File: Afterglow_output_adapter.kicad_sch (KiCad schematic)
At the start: 3 parts, among them J1 Afterglow, J2 Playfield_Col, J3 Playfield_Col

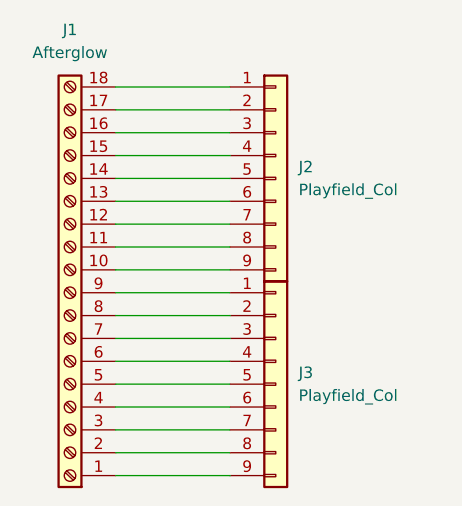
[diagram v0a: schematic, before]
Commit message: Removed unwanted files and changed licence to CC NC
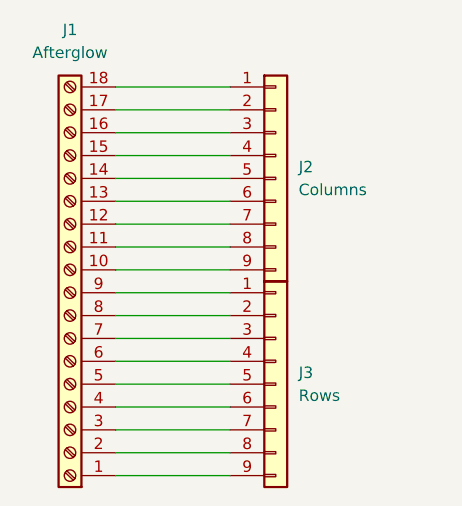
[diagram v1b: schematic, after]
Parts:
- J2: value Playfield_Col -> Columns
- J3: value Playfield_Col -> Rows
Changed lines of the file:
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@@
       (effects (font (size 1.27 1.27)) (justify left))
     )
-    (property "Value" "Playfield_Col" (at 48.26 35.56 0)
+    (property "Value" "Columns" (at 48.26 35.56 0)
       (effects (font (size 1.27 1.27)) (justify left))
     )
@@
       (effects (font (size 1.27 1.27)) (justify left))
     )
-    (property "Value" "Playfield_Col" (at 48.26 58.42 0)
+    (property "Value" "Rows" (at 48.26 58.42 0)
       (effects (font (size 1.27 1.27)) (justify left))
     )
